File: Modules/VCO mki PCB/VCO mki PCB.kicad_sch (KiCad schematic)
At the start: 0 parts

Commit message: wip
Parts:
- added J1, J2, J3, J4: TS_Jack_6.35mm_Sw, SynthStuff:CUI_MJ-63052A, symbol SynthStuff:TS_Jack_6.35mm_Sw
- added R1, R3, R4: 100k, Resistor_THT:R_Axial_DIN0204_L3.6mm_D1.6mm_P5.08mm_Horizontal, symbol Device:R_US
- added R2: 33k, Resistor_THT:R_Axial_DIN0204_L3.6mm_D1.6mm_P5.08mm_Horizontal, symbol Device:R_US
- added R5: 1M, Resistor_THT:R_Axial_DIN0204_L3.6mm_D1.6mm_P5.08mm_Horizontal, symbol Device:R_US
- added RV1, RV2: 100k, Potentiometer_THT:Potentiometer_Alpha_RD901F-40-00D_Single_Vertical, symbol Device:R_Potentiometer_US
- added TH1, TH2: 10k, Resistor_THT:R_Axial_DIN0204_L3.6mm_D1.6mm_P5.08mm_Horizontal, symbol Device:Thermistor_US
- added U1: 40106, Package_DIP:DIP-14_W7.62mm_Socket, symbol 4xxx:40106
- added U2: TL074, Package_DIP:DIP-14_W7.62mm_Socket, symbol Amplifier_Operational:TL074
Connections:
- new net: R1.2, RV1.1
- new net: R3.1, RV1.2
- new net: R2.1, RV1.3
- new net: R5.1, RV2.2
- new net: R5.2, TH2.1
- new net: R3.2, TH1.1
- new net: R4.1, RV2.3
- new net +12V: R1.1
- new net -12V: R2.2, R4.2
- new net GND: RV2.1

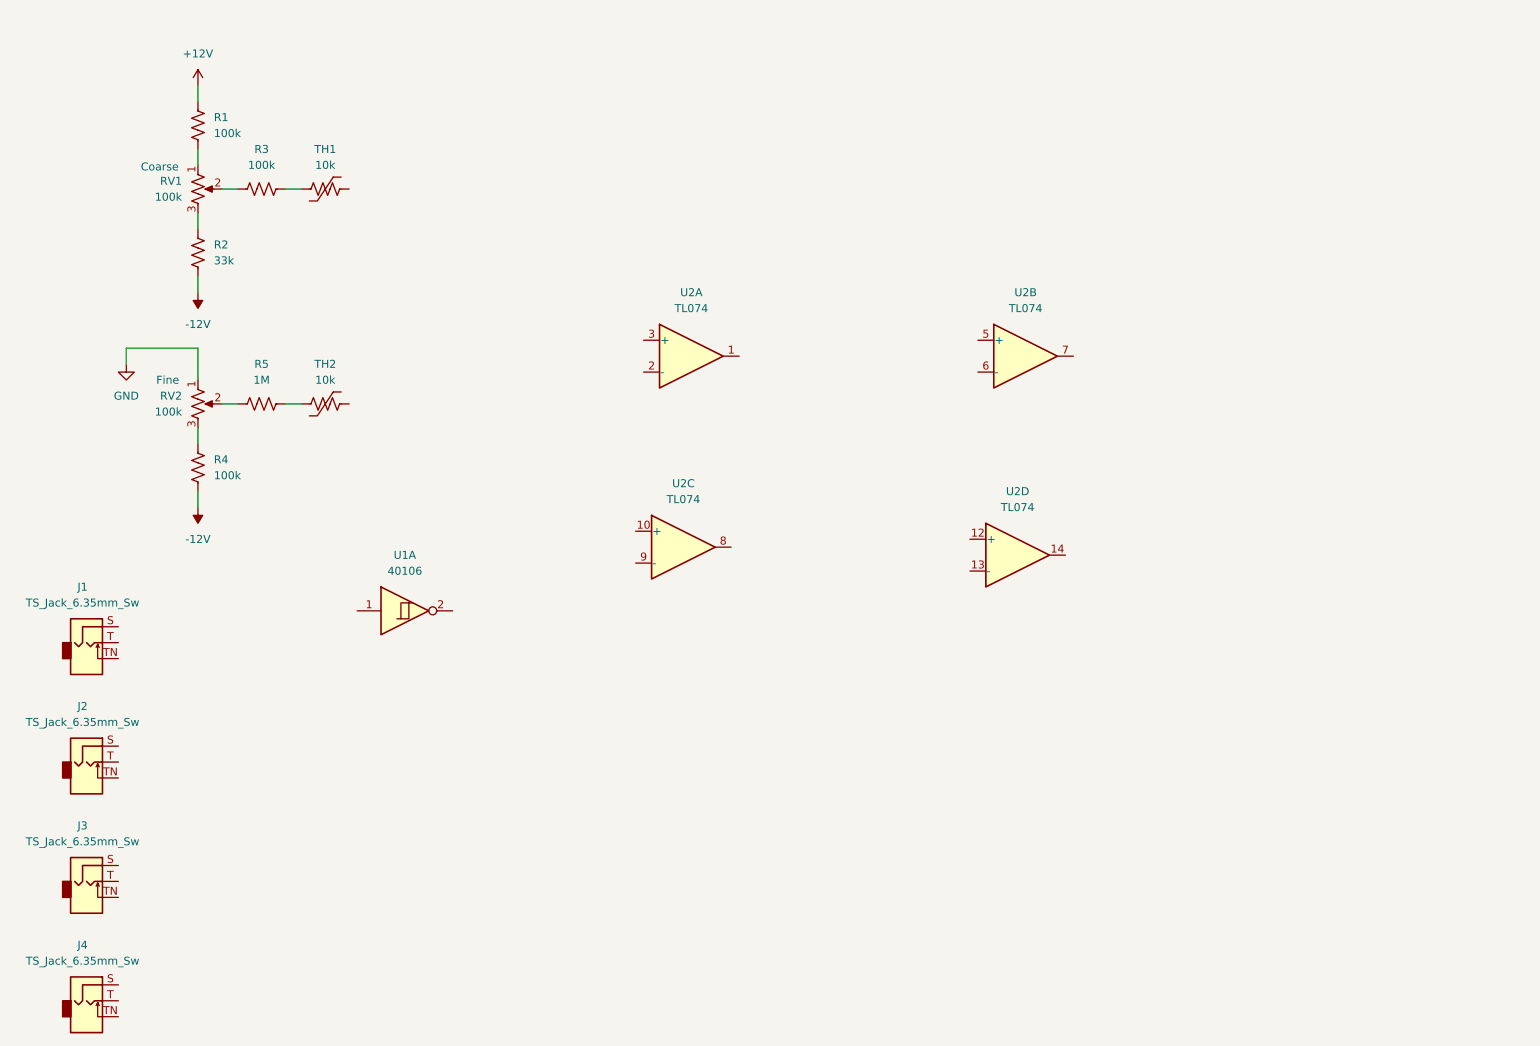
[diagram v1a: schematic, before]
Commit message: Created VCO sub sheets
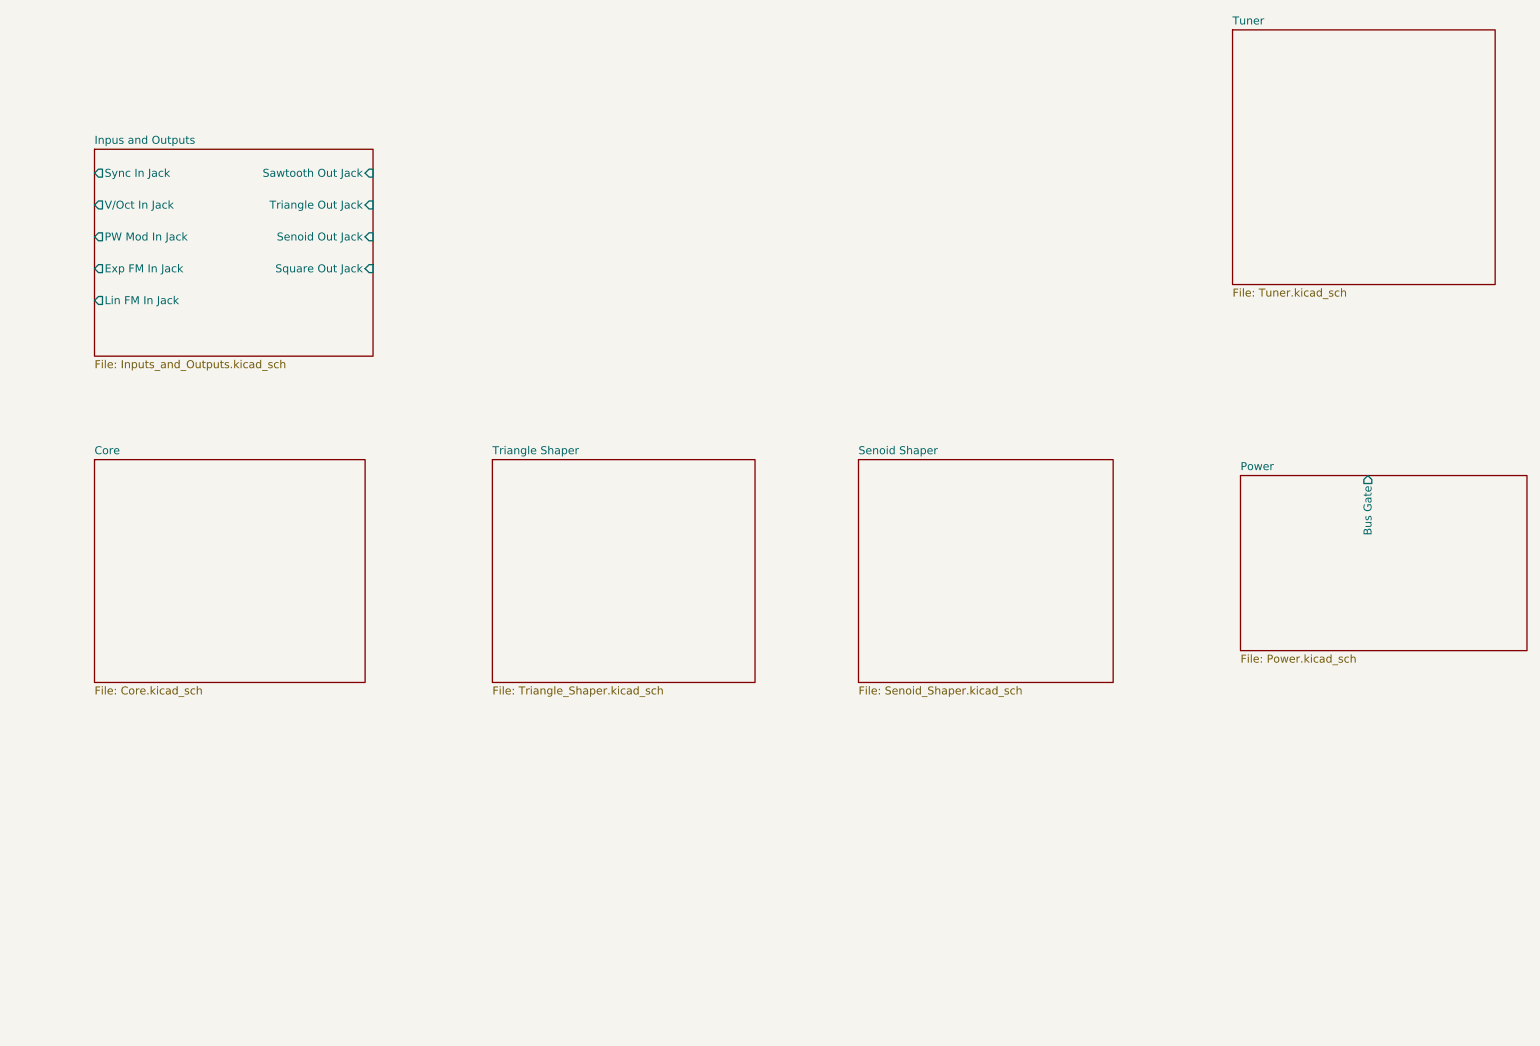
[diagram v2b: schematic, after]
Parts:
- removed J1, J2, J3, J4: TS_Jack_6.35mm_Sw, SynthStuff:CUI_MJ-63052A, symbol SynthStuff:TS_Jack_6.35mm_Sw
- removed R1, R3, R4: 100k, Resistor_THT:R_Axial_DIN0204_L3.6mm_D1.6mm_P5.08mm_Horizontal, symbol Device:R_US
- removed R2: 33k, Resistor_THT:R_Axial_DIN0204_L3.6mm_D1.6mm_P5.08mm_Horizontal, symbol Device:R_US
- removed R5: 1M, Resistor_THT:R_Axial_DIN0204_L3.6mm_D1.6mm_P5.08mm_Horizontal, symbol Device:R_US
- removed RV1, RV2: 100k, Potentiometer_THT:Potentiometer_Alpha_RD901F-40-00D_Single_Vertical, symbol Device:R_Potentiometer_US
- removed TH1, TH2: 10k, Resistor_THT:R_Axial_DIN0204_L3.6mm_D1.6mm_P5.08mm_Horizontal, symbol Device:Thermistor_US
- removed U1: 40106, Package_DIP:DIP-14_W7.62mm_Socket, symbol 4xxx:40106
- removed U2: TL074, Package_DIP:DIP-14_W7.62mm_Socket, symbol Amplifier_Operational:TL074
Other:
- added sheet Core (Core.kicad_sch)
- added sheet Inpus and Outputs (Inputs_and_Outputs.kicad_sch)
- added sheet Power (Power.kicad_sch)
- added sheet Senoid Shaper (Senoid_Shaper.kicad_sch)
- added sheet Triangle Shaper (Triangle_Shaper.kicad_sch)
- added sheet Tuner (Tuner.kicad_sch)

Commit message: Designed VCO core and saw-to-tri circuits
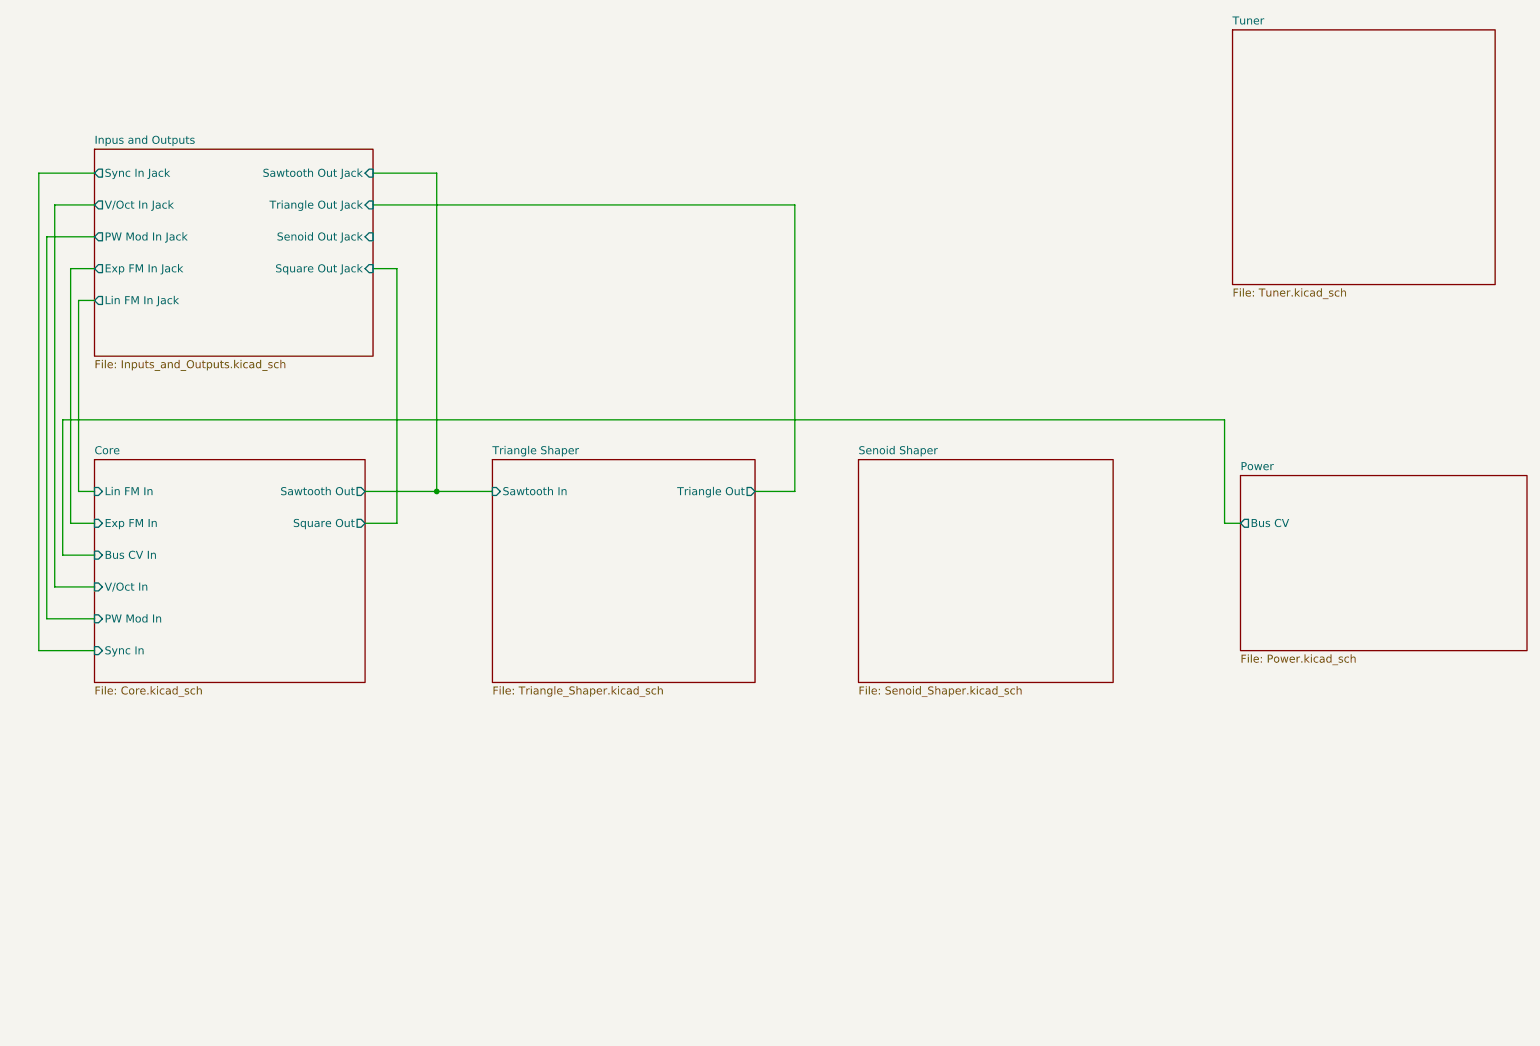
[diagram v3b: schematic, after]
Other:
- sheet Core ports: added Bus CV In, Exp FM In, Lin FM In, PW Mod In, Sawtooth Out, Square Out, Sync In, V/Oct In; removed none
- sheet Power ports: added Bus CV; removed Bus Gate
- sheet Triangle Shaper ports: added Sawtooth In, Triangle Out; removed none

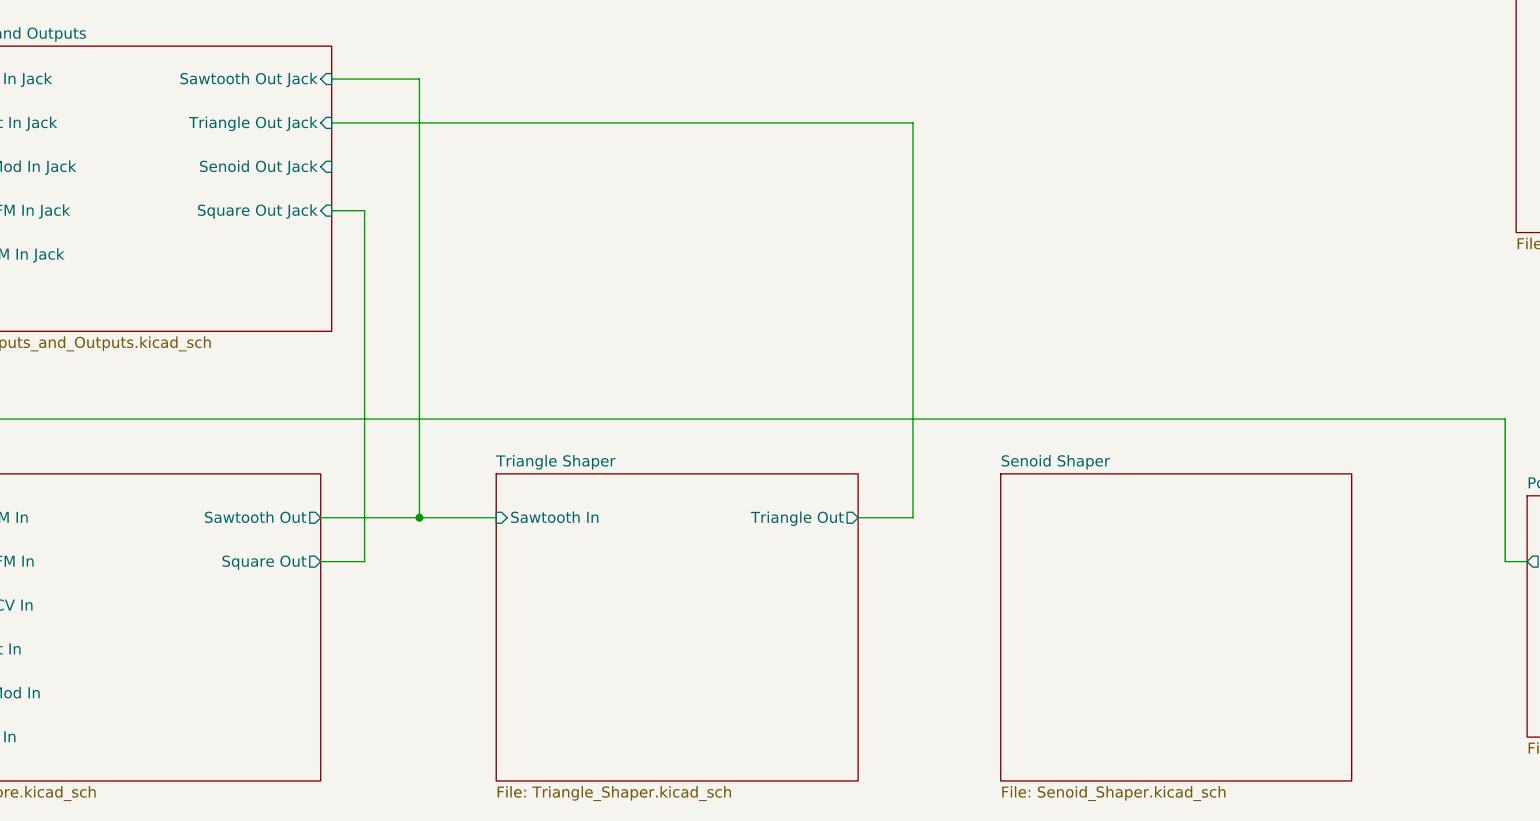
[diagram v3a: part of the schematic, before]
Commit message: Designed Sine Shaper circuit
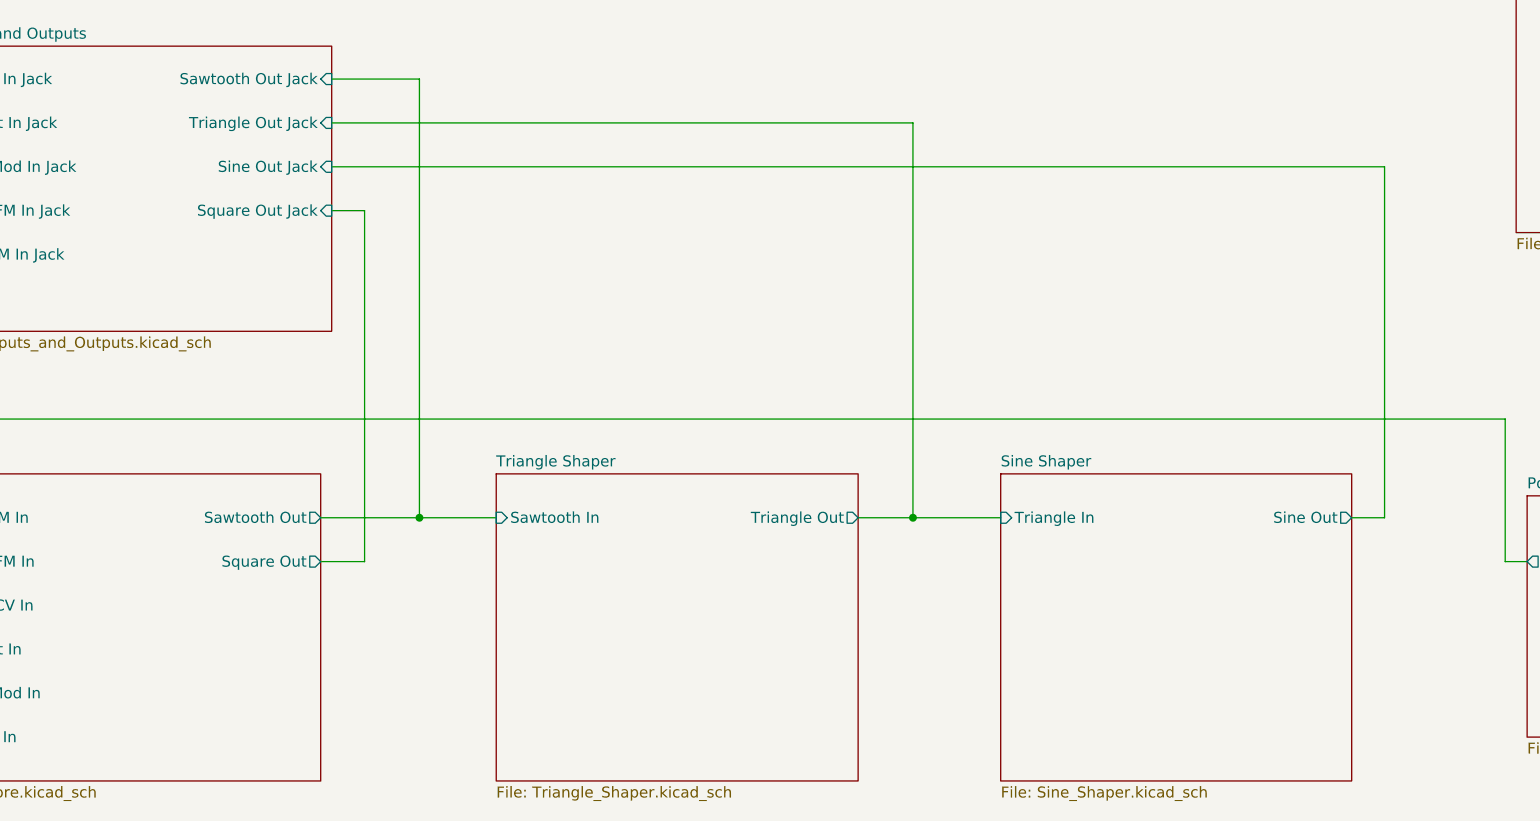
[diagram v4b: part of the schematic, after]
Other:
- sheet Senoid Shaper renamed Sine Shaper
- sheet Inpus and Outputs ports: added Sine Out Jack; removed Senoid Out Jack
- sheet Sine Shaper: file Senoid_Shaper.kicad_sch -> Sine_Shaper.kicad_sch
- sheet Sine Shaper ports: added Sine Out, Triangle In; removed none
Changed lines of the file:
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@@
+	)
+	(junction
+		(at 139.7 104.14)
+		(diameter 0)
+		(color 0 0 0 0)
 	)
 	(junction
@@
 	(wire
 		(pts
+			(xy 194.31 104.14) (xy 194.31 63.5)
+		)
+		(stroke
+			(width 0)
+			(type default)
+		)
+	)
+	(wire
+		(pts
 			(xy 208.28 92.71) (xy 208.28 109.22)
 		)
@@
 	(wire
 		(pts
+			(xy 139.7 104.14) (xy 149.86 104.14)
+		)
+		(stroke
+			(width 0)
+			(type default)
+		)
+	)
+	(wire
+		(pts
 			(xy 82.55 104.14) (xy 91.44 104.14)
 		)
@@
 		(pts
 			(xy 27.94 114.3) (xy 22.86 114.3)
+		)
+		(stroke
+			(width 0)
+			(type default)
+		)
+	)
+	(wire
+		(pts
+			(xy 194.31 63.5) (xy 72.39 63.5)
+		)
+		(stroke
+			(width 0)
+			(type default)
+		)
+	)
+	(wire
+		(pts
+			(xy 190.5 104.14) (xy 194.31 104.14)
 		)
 		(stroke
@@
 			(color 0 0 0 0.0000)
 		)
-		(property "Sheetname" "Senoid Shaper"
+		(property "Sheetname" "Sine Shaper"
 			(at 149.86 98.3484 0)
 			(effects
@@
 			)
 		)
-		(property "Sheetfile" "Senoid_Shaper.kicad_sch"
+		(property "Sheetfile" "Sine_Shaper.kicad_sch"
 			(at 149.86 135.2046 0)
 			(effects
@@
 				)
 				(justify left top)
+			)
+		)
+		(pin "Sine Out" output
+			(at 190.5 104.14 0)
+			(effects
+				(font
+					(size 1.27 1.27)
+				)
+				(justify right)
+			)
+		)
+		(pin "Triangle In" input
+			(at 149.86 104.14 180)
+			(effects
+				(font
+					(size 1.27 1.27)
+				)
+				(justify left)
 			)
 		)
@@
 			)
 		)
-		(pin "Senoid Out Jack" input
+		(pin "Sine Out Jack" input
 			(at 72.39 63.5 0)
 			(effects
